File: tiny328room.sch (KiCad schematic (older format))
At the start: 17 parts, among them K1 PIR, K2 SOIL, U1 DS18B20, U2 DHT11, U3 TINY328, U4 APDS-9006-020

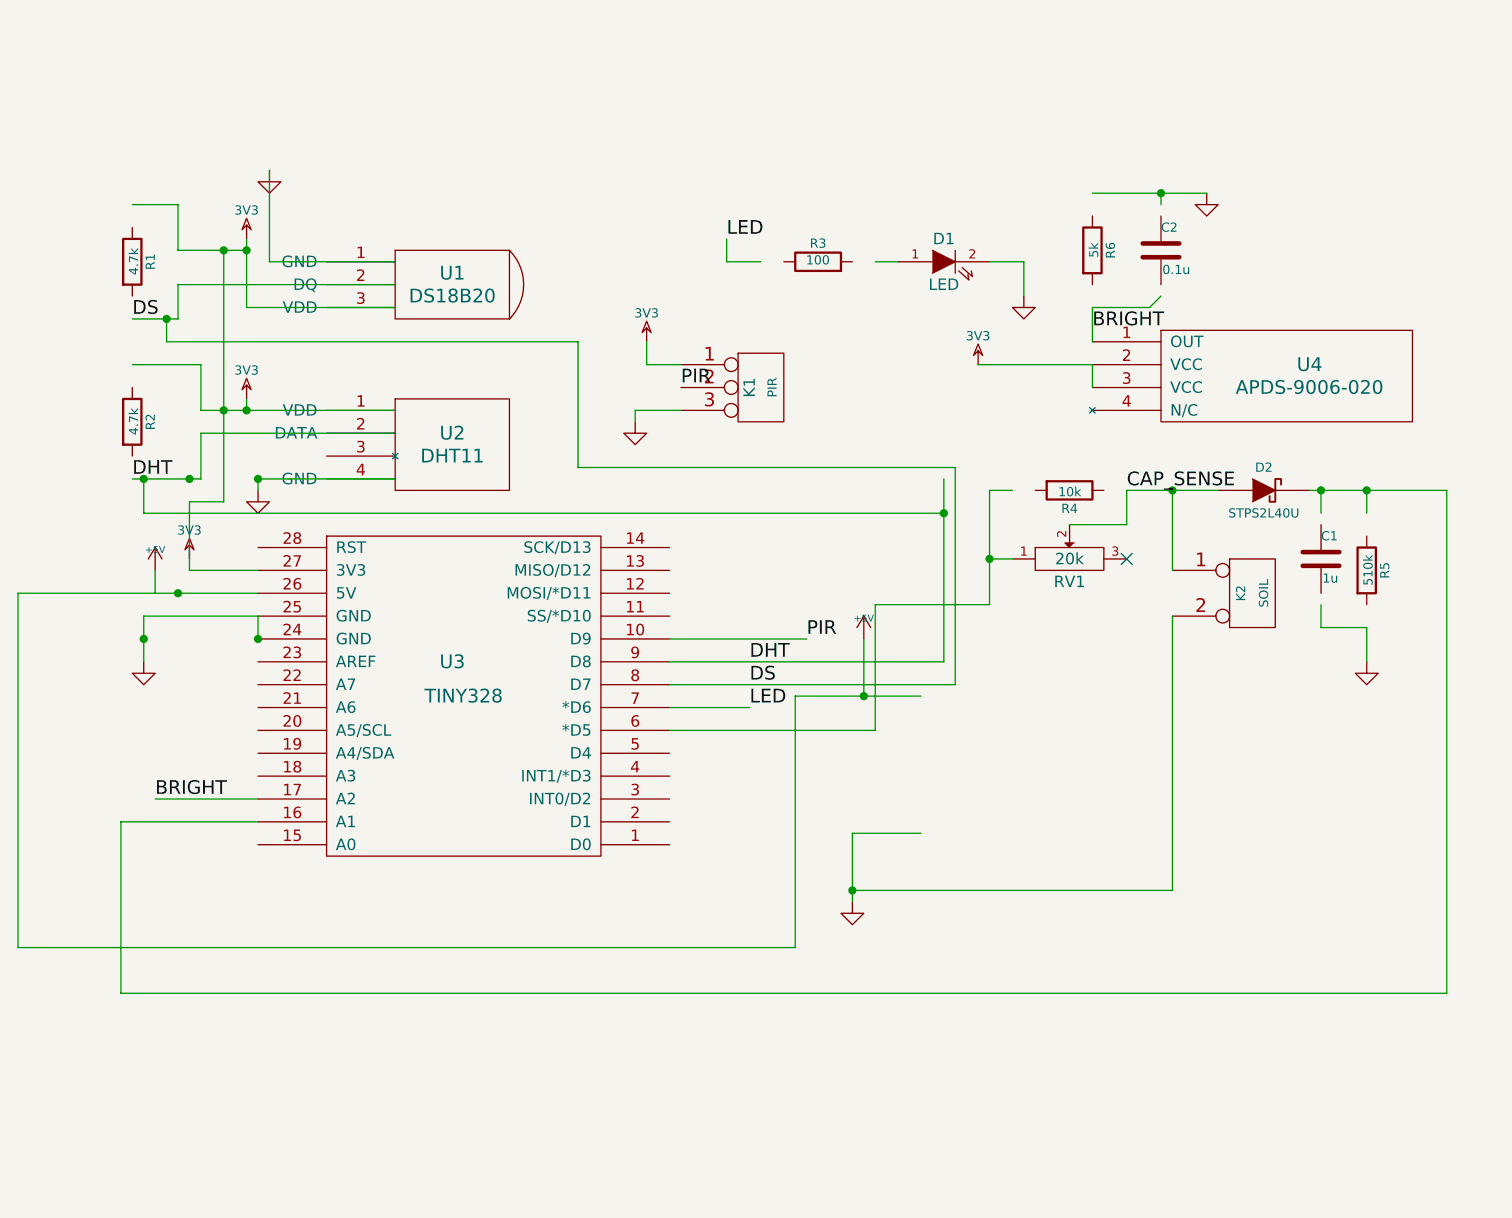
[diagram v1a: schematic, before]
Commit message: added ultrasonic distance measurer
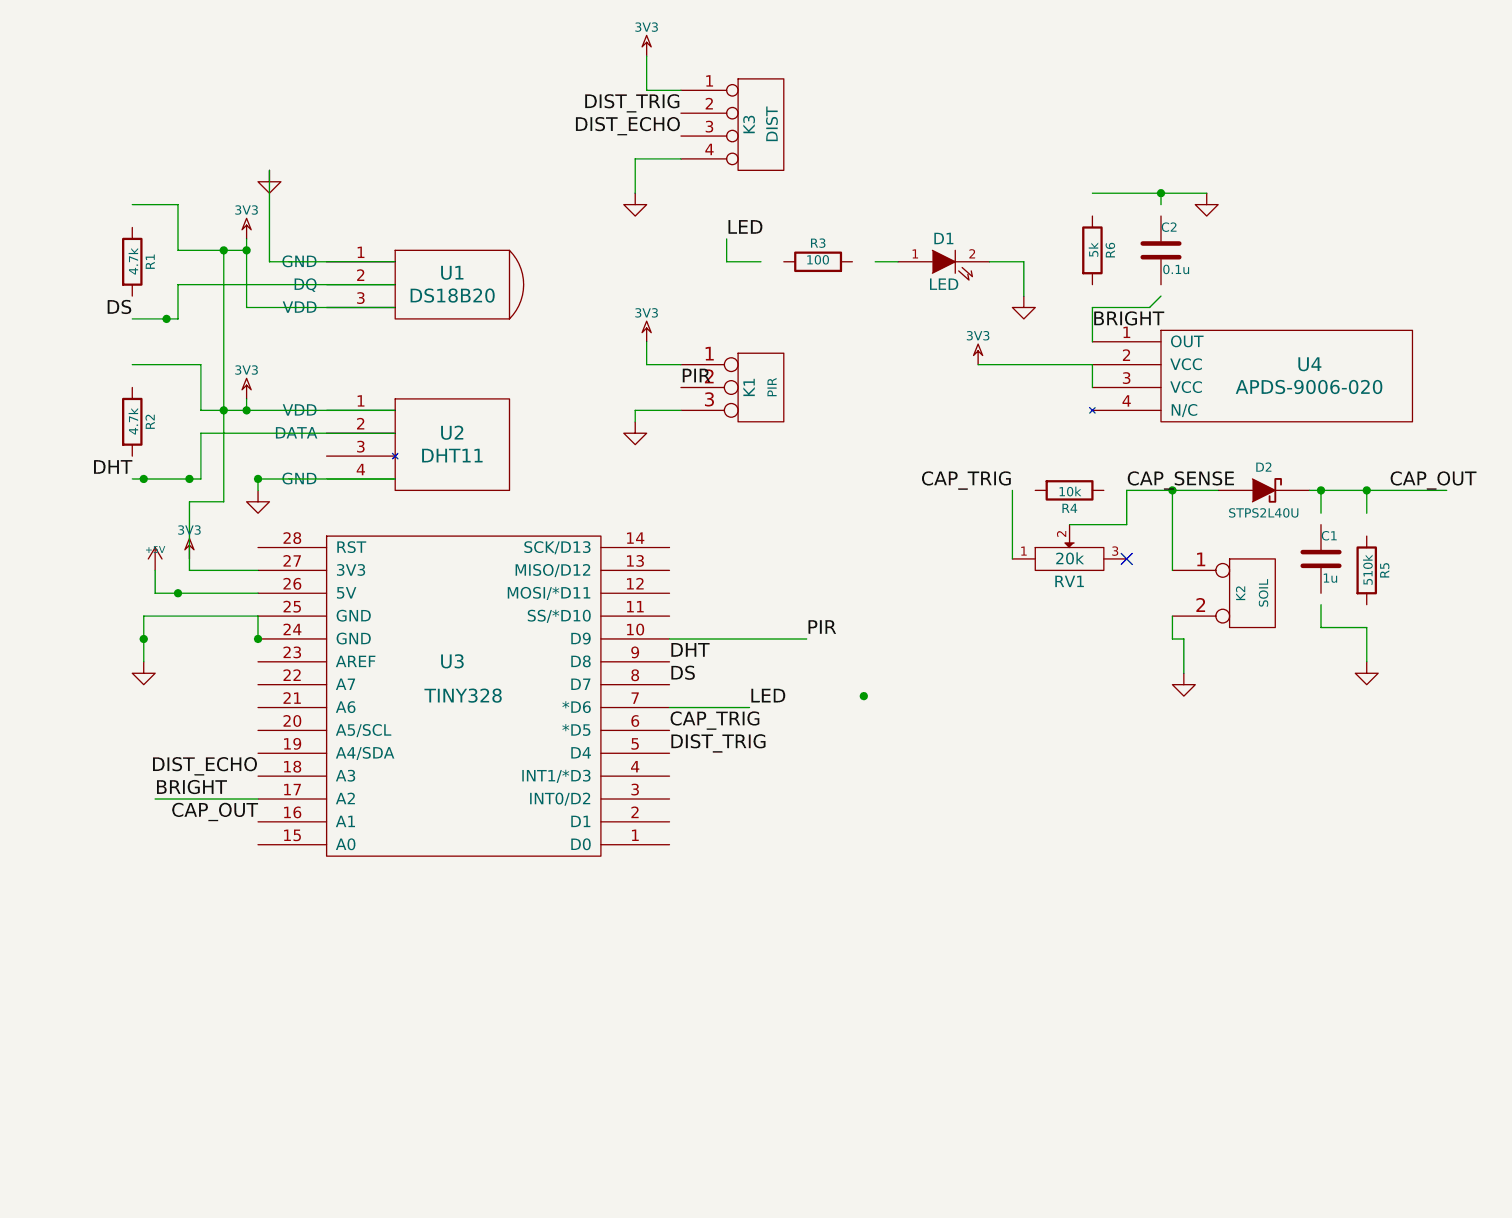
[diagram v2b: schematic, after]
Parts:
- added K3: DIST, ~, symbol CONN_4
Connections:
- net labels added: CAP_OUT, CAP_TRIG, DIST_ECHO, DIST_TRIG
- wire segments 86 -> 66
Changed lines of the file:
@@
 Sheet 1 1
 Title ""
-Date "22 feb 2015"
+Date "20 mar 2015"
 Rev ""
 Comp ""
@@
 L GND #PWR10
 U 1 1 5454FBFF
-P 6300 5200
-F 0 "#PWR10" H 6300 5200 30  0001 C CNN
-F 1 "GND" H 6300 5130 30  0001 C CNN
-F 2 "" H 6300 5200 60  0000 C CNN
-F 3 "" H 6300 5200 60  0000 C CNN
-	1    6300 5200
-	1    0    0    -1
-$EndComp
-Wire Wire Line
-	6600 4900 6300 4900
-Wire Wire Line
-	6300 4900 6300 5200
-Wire Wire Line
-	6050 4300 6600 4300
-Wire Wire Line
-	6350 4300 6350 4050
-$Comp
-L +5V #PWR11
-U 1 1 5454FC2C
-P 6350 4050
-F 0 "#PWR11" H 6350 4140 20  0001 C CNN
-F 1 "+5V" H 6350 4140 30  0000 C CNN
-F 2 "" H 6350 4050 60  0000 C CNN
-F 3 "" H 6350 4050 60  0000 C CNN
-	1    6350 4050
+P 7750 4200
+F 0 "#PWR10" H 7750 4200 30  0001 C CNN
+F 1 "GND" H 7750 4130 30  0001 C CNN
+F 2 "" H 7750 4200 60  0000 C CNN
+F 3 "" H 7750 4200 60  0000 C CNN
+	1    7750 4200
 	1    0    0    -1
 $EndComp
@@
 	3350 2350 3650 2350
 Connection ~ 3650 2350
-Text Label 3150 2650 0    60   ~ 0
+Text Label 3150 2650 2    60   ~ 0
 DS
-Text Label 3150 3350 0    60   ~ 0
+Text Label 3150 3350 2    60   ~ 0
 DHT
-Wire Wire Line
-	7700 3950 7700 5150
-Wire Wire Line
-	7700 5150 6300 5150
-Connection ~ 6300 5150
 $Comp
 L R R3
@@
 Text Label 5550 2950 0    60   ~ 0
 PIR
-Text Label 5850 4150 0    60   ~ 0
+Text Label 5500 4150 0    60   ~ 0
 DHT
-Text Label 5850 4250 0    60   ~ 0
+Text Label 5500 4250 0    60   ~ 0
 DS
 Text Label 5850 4350 0    60   ~ 0
@@
 Connection ~ 3550 3050
 Connection ~ 3550 2350
-Wire Wire Line
-	6700 3350 6700 4150
 Connection ~ 3400 3350
-Wire Wire Line
-	3300 2650 3300 2750
-Wire Wire Line
-	3300 2750 5100 2750
-Wire Wire Line
-	5100 2750 5100 3300
-Wire Wire Line
-	5100 3300 6750 3300
-Wire Wire Line
-	6750 3300 6750 4250
 Connection ~ 3300 2650
-Wire Wire Line
-	6700 3500 3200 3500
-Wire Wire Line
-	3200 3500 3200 3350
 Connection ~ 3200 3350
-Connection ~ 6700 3500
-Wire Wire Line
-	6050 4300 6050 5400
-Wire Wire Line
-	6050 5400 2650 5400
-Wire Wire Line
-	2650 5400 2650 3850
-Wire Wire Line
-	2650 3850 3700 3850
 Connection ~ 3350 3850
 Connection ~ 6350 4300
@@
 	7500 3400 7900 3400
 Wire Wire Line
-	7000 3400 6900 3400
-Wire Wire Line
-	6900 3400 6900 3900
-Wire Wire Line
-	6900 3900 6400 3900
-Wire Wire Line
-	6400 3900 6400 4450
-Wire Wire Line
-	8900 3400 8900 5600
-Wire Wire Line
-	8900 5600 3100 5600
-Wire Wire Line
-	3100 5600 3100 4850
+	7000 3400 7000 3400
 Connection ~ 8550 3400
 Text Label 7500 3400 0    60   ~ 0
@@
 	8350 4000 8550 4000
 Wire Wire Line
-	6900 3700 7000 3700
-Connection ~ 6900 3700
-Wire Wire Line
 	7250 3550 7500 3550
 Wire Wire Line
@@
 	5500 4050 6100 4050
 Wire Wire Line
-	6700 4150 5500 4150
-Wire Wire Line
-	6750 4250 5500 4250
-Wire Wire Line
 	5500 4350 5850 4350
-Wire Wire Line
-	6400 4450 5500 4450
-Wire Wire Line
-	3100 4850 3700 4850
 $Comp
 L CONN_2 K2
@@
 $EndComp
 Wire Wire Line
-	7850 2100 7350 2100
+	7350 2100 7850 2100
 Text Label 7350 2700 0    60   ~ 0
 BRIGHT
@@
 	7650 2150 7650 2100
 Connection ~ 7650 2100
+$Comp
+L CONN_4 K3
+U 1 1 550C1E9C
+P 5900 1800
+F 0 "K3" V 5850 1800 50  0000 C CNN
+F 1 "DIST" V 5950 1800 50  0000 C CNN
+F 2 "~" H 5900 1800 60  0000 C CNN
+F 3 "~" H 5900 1800 60  0000 C CNN
+	1    5900 1800
+	1    0    0    -1
+$EndComp
+$Comp
+L 3V3 #PWR?
+U 1 1 550C1EBC
+P 5400 1500
+F 0 "#PWR?" H 5400 1600 40  0001 C CNN
+F 1 "3V3" H 5400 1625 40  0000 C CNN
+F 2 "" H 5400 1500 60  0000 C CNN
+F 3 "" H 5400 1500 60  0000 C CNN
+	1    5400 1500
+	1    0    0    -1
+$EndComp
+$Comp
+L GND #PWR?
+U 1 1 550C1EC2
+P 5350 2100
+F 0 "#PWR?" H 5350 2100 30  0001 C CNN
+F 1 "GND" H 5350 2030 30  0001 C CNN
+F 2 "" H 5350 2100 60  0000 C CNN
+F 3 "" H 5350 2100 60  0000 C CNN
+	1    5350 2100
+	1    0    0    -1
+$EndComp
+Wire Wire Line
+	5350 2100 5350 1950
+Wire Wire Line
+	5350 1950 5550 1950
+Wire Wire Line
+	5550 1650 5400 1650
+Wire Wire Line
+	5400 1650 5400 1500
+Text Label 5550 1750 2    60   ~ 0
+DIST_TRIG
+Text Label 5550 1850 2    60   ~ 0
+DIST_ECHO
+Text Label 8650 3400 0    60   ~ 0
+CAP_OUT
+Text Label 5500 4450 0    60   ~ 0
+CAP_TRIG
+Text Label 7000 3400 2    60   ~ 0
+CAP_TRIG
+Wire Wire Line
+	7000 3700 7000 3400
+Text Label 3700 4850 2    60   ~ 0
+CAP_OUT
+Wire Wire Line
+	7700 3950 7700 4050
+Wire Wire Line
+	7700 4050 7750 4050
+Wire Wire Line
+	7750 4050 7750 4200
+Wire Wire Line
+	3250 3850 3700 3850
+Text Label 5500 4550 0    60   ~ 0
+DIST_TRIG
+Text Label 3700 4650 2    60   ~ 0
+DIST_ECHO
 $EndSCHEMATC

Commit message: add resistors to FET for stability
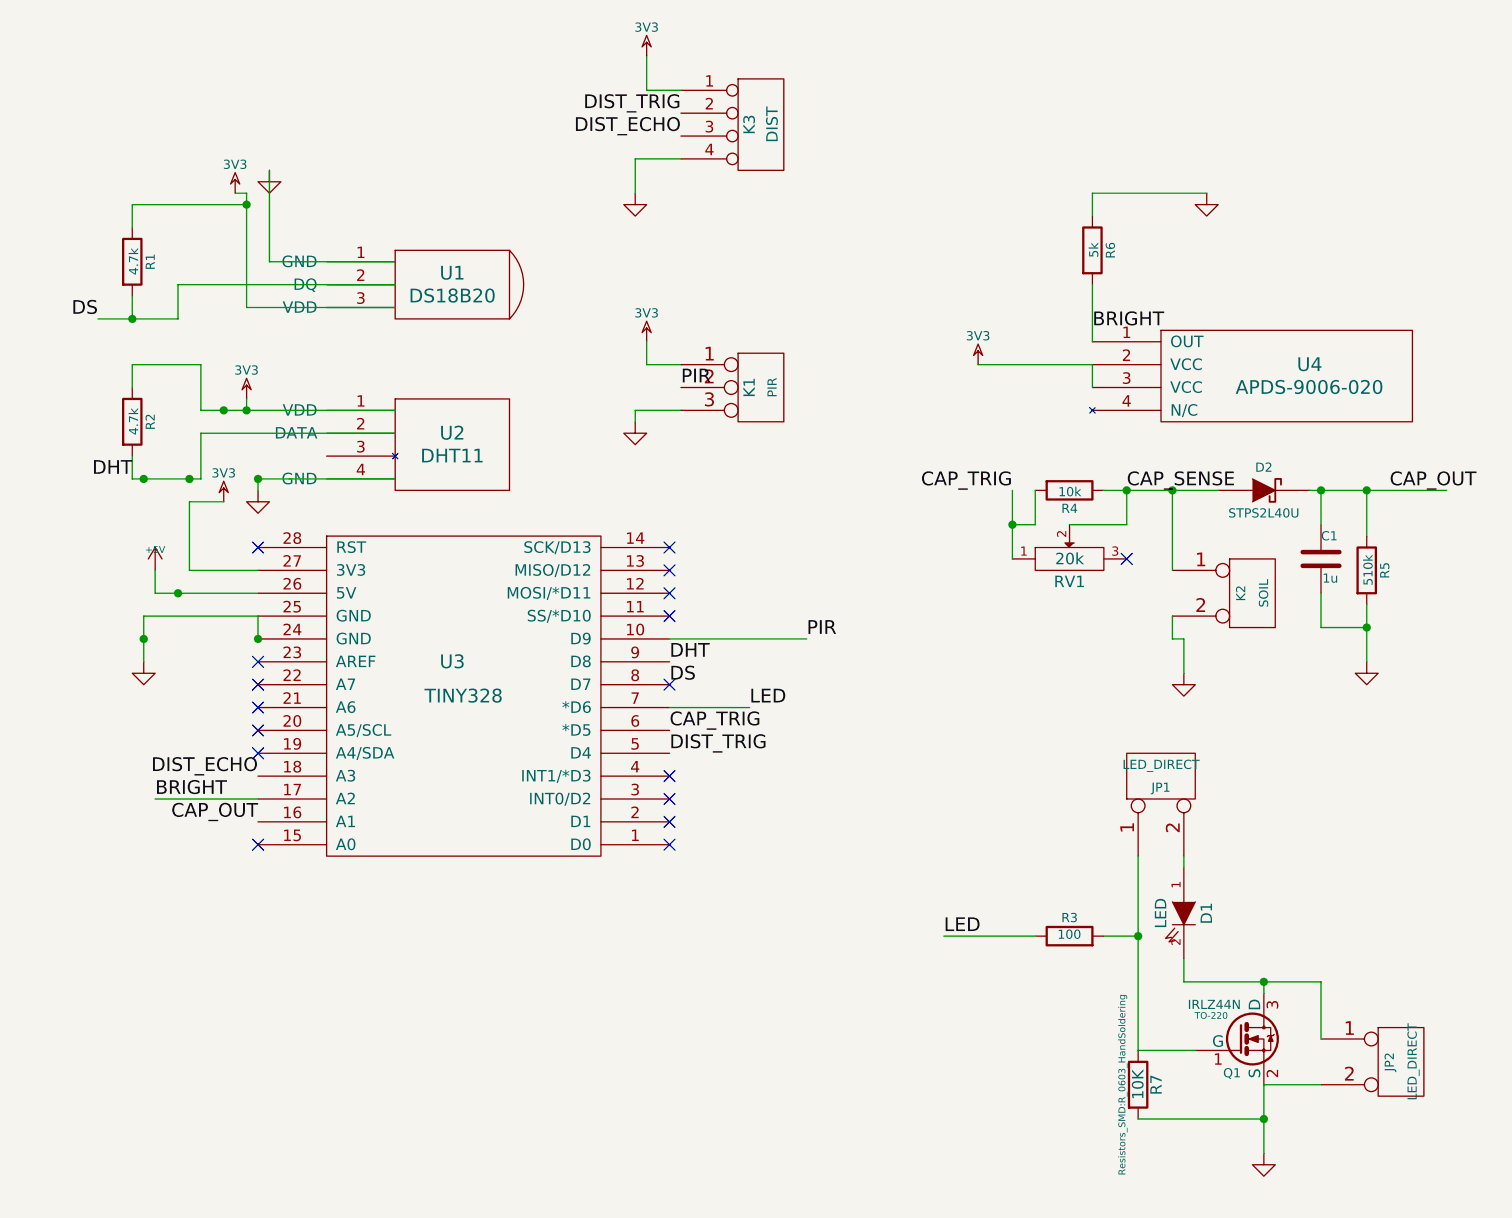
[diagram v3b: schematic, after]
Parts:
- removed C2: 0.1u, ~, symbol C
- added JP1, JP2: LED_DIRECT, ~, symbol CONN_2
- added Q1: IRLZ44N, TO-220, symbol BSS138
- added R7: 10K, Resistors_SMD:R_0603_HandSoldering, symbol R
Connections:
- wire segments 66 -> 75
- no-connect marks 1 -> 17
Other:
- moved on the sheet: D1, R3
